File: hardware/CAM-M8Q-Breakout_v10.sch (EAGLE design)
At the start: 20 parts, among them J2 MA06-1, J3 MA06-1, X1 PASSER-07, X2 PASSER-07, X3 PASSER-07, X4 PASSER-07

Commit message: updated layout and schematics
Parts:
- removed J3: MA06-1, we-con:MA06-1
- added J1: MA06-1, we-con:MA06-1
- R1, R2: value (none) -> nc
- R3: value (none) -> 0
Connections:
- net EXT_INT: now also J2.5; no longer J3.5
- net GND: now also J1.2; no longer J2.2
- net LNA_EN: now also J2.4; no longer J3.4
- net RESET: now also J2.2; no longer J3.2
- net RXD: now also J1.4; no longer J2.4
- net SAFEBOOT: now also J2.3; no longer J3.3
- net SCL: now also J1.5; no longer J2.5
- net SDA: now also J1.6; no longer J2.6
- net TIMEPULS: now also J2.6; no longer J3.6
- net TXD: now also J1.3; no longer J2.3
- net VCC: now also J1.1; no longer J2.1
- net VIO: now also J2.1; no longer J3.1
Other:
- moved on the sheet: BAT, J2, OUT, R2, R3

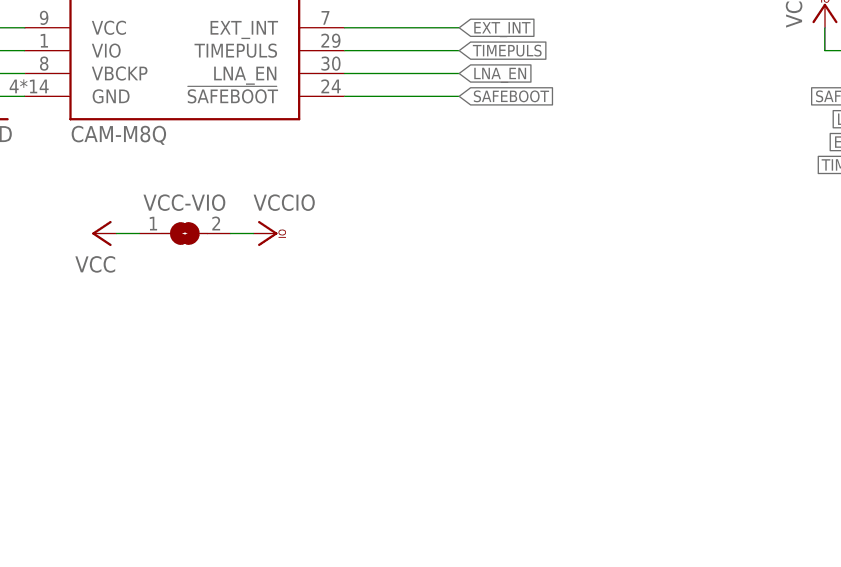
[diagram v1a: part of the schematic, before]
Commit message: updated schematics
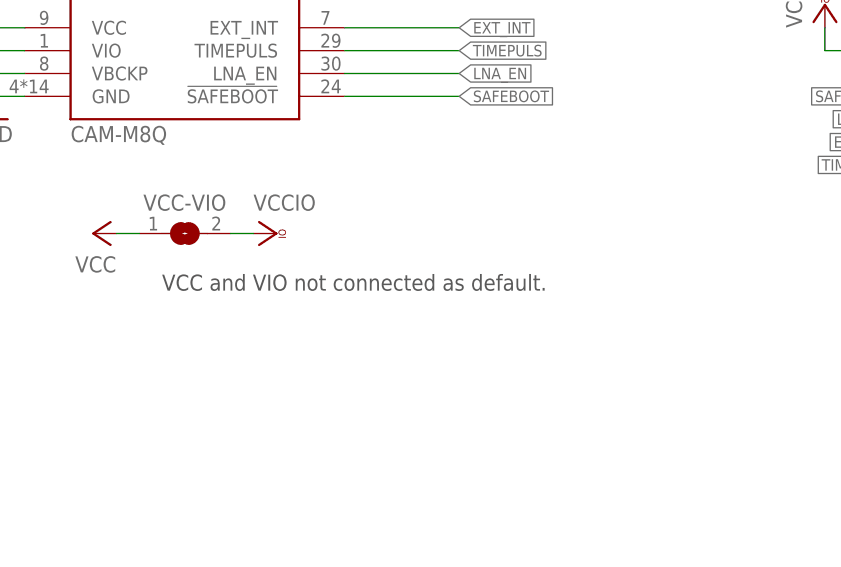
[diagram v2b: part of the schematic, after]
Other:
- note added: "VCC and VIO not connected as default."
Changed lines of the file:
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@@
 <setting verticaltext="up"/>
 </settings>
-<grid distance="0.05" unitdist="inch" unit="inch" style="lines" multiple="1" display="yes" altdistance="0.025" altunitdist="inch" altunit="inch"/>
+<grid distance="0.05" unitdist="inch" unit="inch" style="lines" multiple="1" display="yes" altdistance="0.01" altunitdist="inch" altunit="inch"/>
 <layers>
 <layer number="1" name="Top" color="4" fill="1" visible="no" active="no"/>
@@
 License. http://creativecommons.org/licenses/by-sa/4.0/
 Designed by Watterott electronic</text>
+<text x="111.76" y="73.66" size="1.778" layer="97">VCC and VIO not connected as default.</text>
 </plain>
 <instances>
